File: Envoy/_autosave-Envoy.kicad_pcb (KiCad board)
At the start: 2 copper layers, 95.4 x 95.4 mm, 57 parts

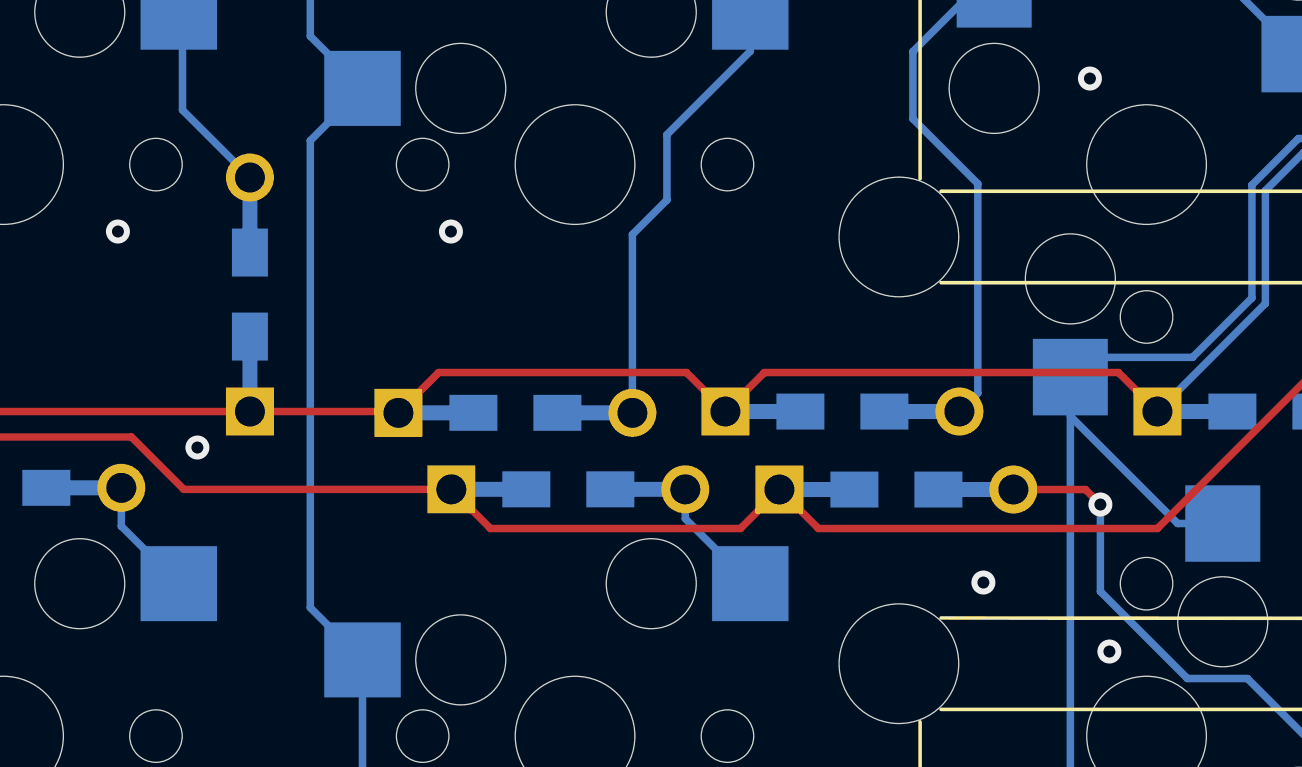
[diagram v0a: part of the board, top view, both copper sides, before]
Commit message: update git ignore to not keep autosaves
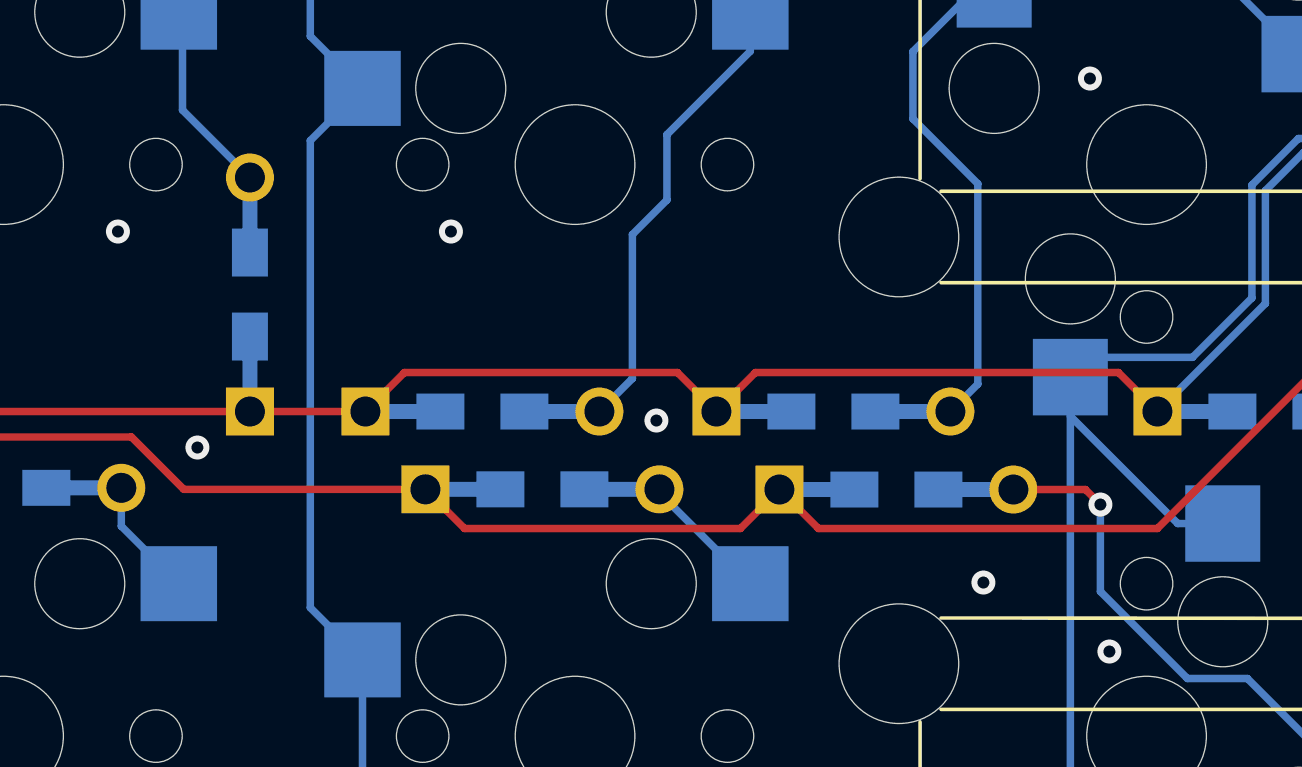
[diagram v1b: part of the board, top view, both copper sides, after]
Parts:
- moved D11 1.10 mm to (144.6, 111.4)
- moved D15 0.86 mm to (146.6, 114.0)
- moved D12 0.30 mm to (156.3, 111.4)
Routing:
- net GND: vias 37 -> 38
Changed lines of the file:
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@@
   )
   (footprint "Envoy:Diode-Hybrid-Back" (layer "F.Cu")
-    (at 145.7 111.44375 180)
+    (at 144.6 111.4 180)
     (attr smd)
     (fp_text reference "D11" (at -0.0254 1.4) (layer "B.SilkS")
@@
   )
   (footprint "Envoy:Diode-Hybrid-Back" (layer "F.Cu")
-    (at 156.6 111.4 180)
+    (at 156.3 111.4 180)
     (attr smd)
     (fp_text reference "D12" (at -0.0254 1.4) (layer "B.SilkS")
@@
   )
   (footprint "Envoy:Diode-Hybrid-Back" (layer "F.Cu")
-    (at 147.4635 113.99375 180)
+    (at 146.6 113.99375 180)
     (attr smd)
     (fp_text reference "D15" (at -0.0254 -1.4) (layer "B.SilkS")
@@
   (segment (start 159.651 70.276) (end 162.775 73.4) (width 0.25) (layer "B.Cu") (net 5))
   (segment (start 159.6535 70.20875) (end 159.651 70.21125) (width 0.25) (layer "B.Cu") (net 5))
-  (segment (start 151.4 110.1) (end 143.14375 110.1) (width 0.25) (layer "F.Cu") (net 6))
-  (segment (start 152.7 111.4) (end 154 110.1) (width 0.25) (layer "F.Cu") (net 6))
   (segment (start 111.9635 101.19375) (end 116.24475 101.19375) (width 0.25) (layer "F.Cu") (net 6))
-  (segment (start 143.14375 110.1) (end 141.8 111.44375) (width 0.25) (layer "F.Cu") (net 6))
-  (segment (start 152.7 111.4) (end 151.4 110.1) (width 0.25) (layer "F.Cu") (net 6))
-  (segment (start 165.8 110.1) (end 167.1 111.4) (width 0.25) (layer "F.Cu") (net 6))
-  (segment (start 154 110.1) (end 165.8 110.1) (width 0.25) (layer "F.Cu") (net 6))
-  (segment (start 141.8 111.44375) (end 141.75625 111.4) (width 0.25) (layer "F.Cu") (net 6))
+  (segment (start 152.4 111.4) (end 153.7 110.1) (width 0.25) (layer "F.Cu") (net 6))
+  (segment (start 153.7 110.1) (end 165.8 110.1) (width 0.25) (layer "F.Cu") (net 6))
+  (segment (start 151.1 110.1) (end 142 110.1) (width 0.25) (layer "F.Cu") (net 6))
+  (segment (start 140.7 111.4) (end 136.851 111.4) (width 0.25) (layer "F.Cu") (net 6))
   (segment (start 105.6635 94.89375) (end 111.9635 101.19375) (width 0.25) (layer "F.Cu") (net 6))
   (segment (start 126.451 111.4) (end 136.851 111.4) (width 0.25) (layer "F.Cu") (net 6))
+  (segment (start 152.4 111.4) (end 151.1 110.1) (width 0.25) (layer "F.Cu") (net 6))
+  (segment (start 142 110.1) (end 140.7 111.4) (width 0.25) (layer "F.Cu") (net 6))
+  (segment (start 165.8 110.1) (end 167.1 111.4) (width 0.25) (layer "F.Cu") (net 6))
   (segment (start 116.24475 101.19375) (end 126.451 111.4) (width 0.25) (layer "F.Cu") (net 6))
-  (segment (start 141.75625 111.4) (end 136.851 111.4) (width 0.25) (layer "F.Cu") (net 6))
   (segment (start 170.7 107.8) (end 167.1 111.4) (width 0.25) (layer "B.Cu") (net 6))
   (segment (start 178.1799 84.849) (end 176.126489 86.902411) (width 0.25) (layer "B.Cu") (net 6))
@@
   (segment (start 171.8185 89.96075) (end 171.8185 90.51375) (width 0.25) (layer "B.Cu") (net 10))
   (segment (start 173.6 108.8) (end 178.6 108.8) (width 0.25) (layer "F.Cu") (net 11))
+  (segment (start 153.2 115.3) (end 154.5 114) (width 0.25) (layer "F.Cu") (net 11))
+  (segment (start 154.5 114) (end 155.8 115.3) (width 0.25) (layer "F.Cu") (net 11))
+  (segment (start 144.00625 115.3) (end 153.2 115.3) (width 0.25) (layer "F.Cu") (net 11))
+  (segment (start 123.0135 112.19375) (end 124.7635 113.94375) (width 0.25) (layer "F.Cu") (net 11))
+  (segment (start 142.7 113.99375) (end 144.00625 115.3) (width 0.25) (layer "F.Cu") (net 11))
+  (segment (start 155.8 115.3) (end 167.1 115.3) (width 0.25) (layer "F.Cu") (net 11))
+  (segment (start 167.1 115.3) (end 173.6 108.8) (width 0.25) (layer "F.Cu") (net 11))
+  (segment (start 134.64475 113.99375) (end 142.7 113.99375) (width 0.25) (layer "F.Cu") (net 11))
+  (segment (start 126.45725 112.25) (end 132.901 112.25) (width 0.25) (layer "F.Cu") (net 11))
+  (segment (start 107.4385 112.19375) (end 123.0135 112.19375) (width 0.25) (layer "F.Cu") (net 11))
   (segment (start 124.7635 113.94375) (end 126.45725 112.25) (width 0.25) (layer "F.Cu") (net 11))
-  (segment (start 154.5 114) (end 155.8 115.3) (width 0.25) (layer "F.Cu") (net 11))
-  (segment (start 143.5635 113.99375) (end 144.86975 115.3) (width 0.25) (layer "F.Cu") (net 11))
-  (segment (start 123.0135 112.19375) (end 124.7635 113.94375) (width 0.25) (layer "F.Cu") (net 11))
-  (segment (start 153.2 115.3) (end 154.5 114) (width 0.25) (layer "F.Cu") (net 11))
   (segment (start 132.901 112.25) (end 134.64475 113.99375) (width 0.25) (layer "F.Cu") (net 11))
-  (segment (start 134.64475 113.99375) (end 143.5635 113.99375) (width 0.25) (layer "F.Cu") (net 11))
-  (segment (start 155.8 115.3) (end 167.1 115.3) (width 0.25) (layer "F.Cu") (net 11))
-  (segment (start 126.45725 112.25) (end 132.901 112.25) (width 0.25) (layer "F.Cu") (net 11))
-  (segment (start 167.1 115.3) (end 173.6 108.8) (width 0.25) (layer "F.Cu") (net 11))
-  (segment (start 144.86975 115.3) (end 153.2 115.3) (width 0.25) (layer "F.Cu") (net 11))
-  (segment (start 107.4385 112.19375) (end 123.0135 112.19375) (width 0.25) (layer "F.Cu") (net 11))
   (segment (start 105.6885 113.94375) (end 107.4385 112.19375) (width 0.25) (layer "F.Cu") (net 11))
   (segment (start 179.651 83.7801) (end 178.1799 82.309) (width 0.25) (layer "B.Cu") (net 11))
@@
   (segment (start 134.60225 101.35125) (end 136.851 103.6) (width 0.25) (layer "B.Cu") (net 13))
   (segment (start 134.60225 98.08875) (end 134.60225 101.35125) (width 0.25) (layer "B.Cu") (net 13))
-  (segment (start 150.751 102.17) (end 150.751 104.349) (width 0.25) (layer "B.Cu") (net 14))
-  (segment (start 149.6 105.5) (end 149.6 111.44375) (width 0.25) (layer "B.Cu") (net 14))
+  (segment (start 150.751 104.349) (end 149.6 105.5) (width 0.25) (layer "B.Cu") (net 14))
+  (segment (start 149.6 110.3) (end 148.5 111.4) (width 0.25) (layer "B.Cu") (net 14))
+  (segment (start 149.6 105.5) (end 149.6 110.3) (width 0.25) (layer "B.Cu") (net 14))
   (segment (start 153.5305 98.08875) (end 153.5305 99.3905) (width 0.25) (layer "B.Cu") (net 14))
   (segment (start 153.5305 99.3905) (end 150.751 102.17) (width 0.25) (layer "B.Cu") (net 14))
-  (segment (start 150.751 104.349) (end 149.6 105.5) (width 0.25) (layer "B.Cu") (net 14))
-  (segment (start 161.1135 103.8075) (end 161.1135 110.7865) (width 0.25) (layer "B.Cu") (net 15))
+  (segment (start 150.751 102.17) (end 150.751 104.349) (width 0.25) (layer "B.Cu") (net 14))
+  (segment (start 161.1135 110.4865) (end 160.2 111.4) (width 0.25) (layer "B.Cu") (net 15))
   (segment (start 161.02425 97.32675) (end 158.951 99.4) (width 0.25) (layer "B.Cu") (net 15))
-  (segment (start 161.1135 110.7865) (end 160.5 111.4) (width 0.25) (layer "B.Cu") (net 15))
   (segment (start 158.951 101.645) (end 161.1135 103.8075) (width 0.25) (layer "B.Cu") (net 15))
+  (segment (start 161.1135 103.8075) (end 161.1135 110.4865) (width 0.25) (layer "B.Cu") (net 15))
   (segment (start 158.951 99.4) (end 158.951 101.645) (width 0.25) (layer "B.Cu") (net 15))
   (segment (start 168.651 130.1) (end 170.251 130.1) (width 0.25) (layer "F.Cu") (net 16))
@@
   (segment (start 134.4805 117.13875) (end 132.5635 115.22175) (width 0.25) (layer "B.Cu") (net 18))
   (segment (start 132.5635 115.22175) (end 132.5635 113.94375) (width 0.25) (layer "B.Cu") (net 18))
-  (segment (start 153.5305 117.13875) (end 151.3635 114.97175) (width 0.25) (layer "B.Cu") (net 19))
-  (segment (start 151.3635 114.97175) (end 151.3635 113.99375) (width 0.25) (layer "B.Cu") (net 19))
+  (segment (start 150.5 114.10825) (end 150.5 113.99375) (width 0.25) (layer "B.Cu") (net 19))
+  (segment (start 153.5305 117.13875) (end 150.5 114.10825) (width 0.25) (layer "B.Cu") (net 19))
   (segment (start 165.2 114.5) (end 164.7 114) (width 0.25) (layer "F.Cu") (net 20))
   (segment (start 164.7 114) (end 162.3 114) (width 0.25) (layer "F.Cu") (net 20))
@@
   (via (at 170.451 83.4) (size 0.8) (drill 0.4) (layers "F.Cu" "B.Cu") (free) (net 31))
   (via (at 113.251 124.4) (size 0.8) (drill 0.4) (layers "F.Cu" "B.Cu") (free) (net 31))
+  (via (at 150.4 111.7) (size 0.8) (drill 0.4) (layers "F.Cu" "B.Cu") (free) (net 31))
   (via (at 143.551 105.4) (size 0.8) (drill 0.4) (layers "F.Cu" "B.Cu") (free) (net 31))
   (via (at 162.451 67.2) (size 0.8) (drill 0.4) (layers "F.Cu" "B.Cu") (free) (net 31))
